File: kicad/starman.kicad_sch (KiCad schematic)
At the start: 244 parts, among them J1 M20-8771246, J10 PJ-063AH, J11 Conn_02x01, J2 M20-8771246, J3 M20-8771246, J4 ESW-106-44-T-S, J5 PH2-06-UA, J6 ESW-112-44-T-S, J7 Conn_01x10, J8 ESW-112-44-T-S, J9 Conn_01x10, SW1 PTS810 SJM 250 SMTR LFS, SW2 PTS810 SJM 250 SMTR LFS, SW3 SW_SPST, U1 ESP32-S2-MINI-1, U10 LED1642GWTTR, U11 AZ1084CS2-ADJ, U12 BA33BC0FP-E2, U13 PAM8302AAS, U2 LED1642GWTTR, U3 LED1642GWTTR, U4 LED1642GWTTR, U5 LED1642GWTTR, U6 LED1642GWTTR, U7 LED1642GWTTR, U8 LED1642GWTTR, U9 LED1642GWTTR, X1 ECS-2333-300, X2 ECS-2333-300, X3 ECS-2333-300

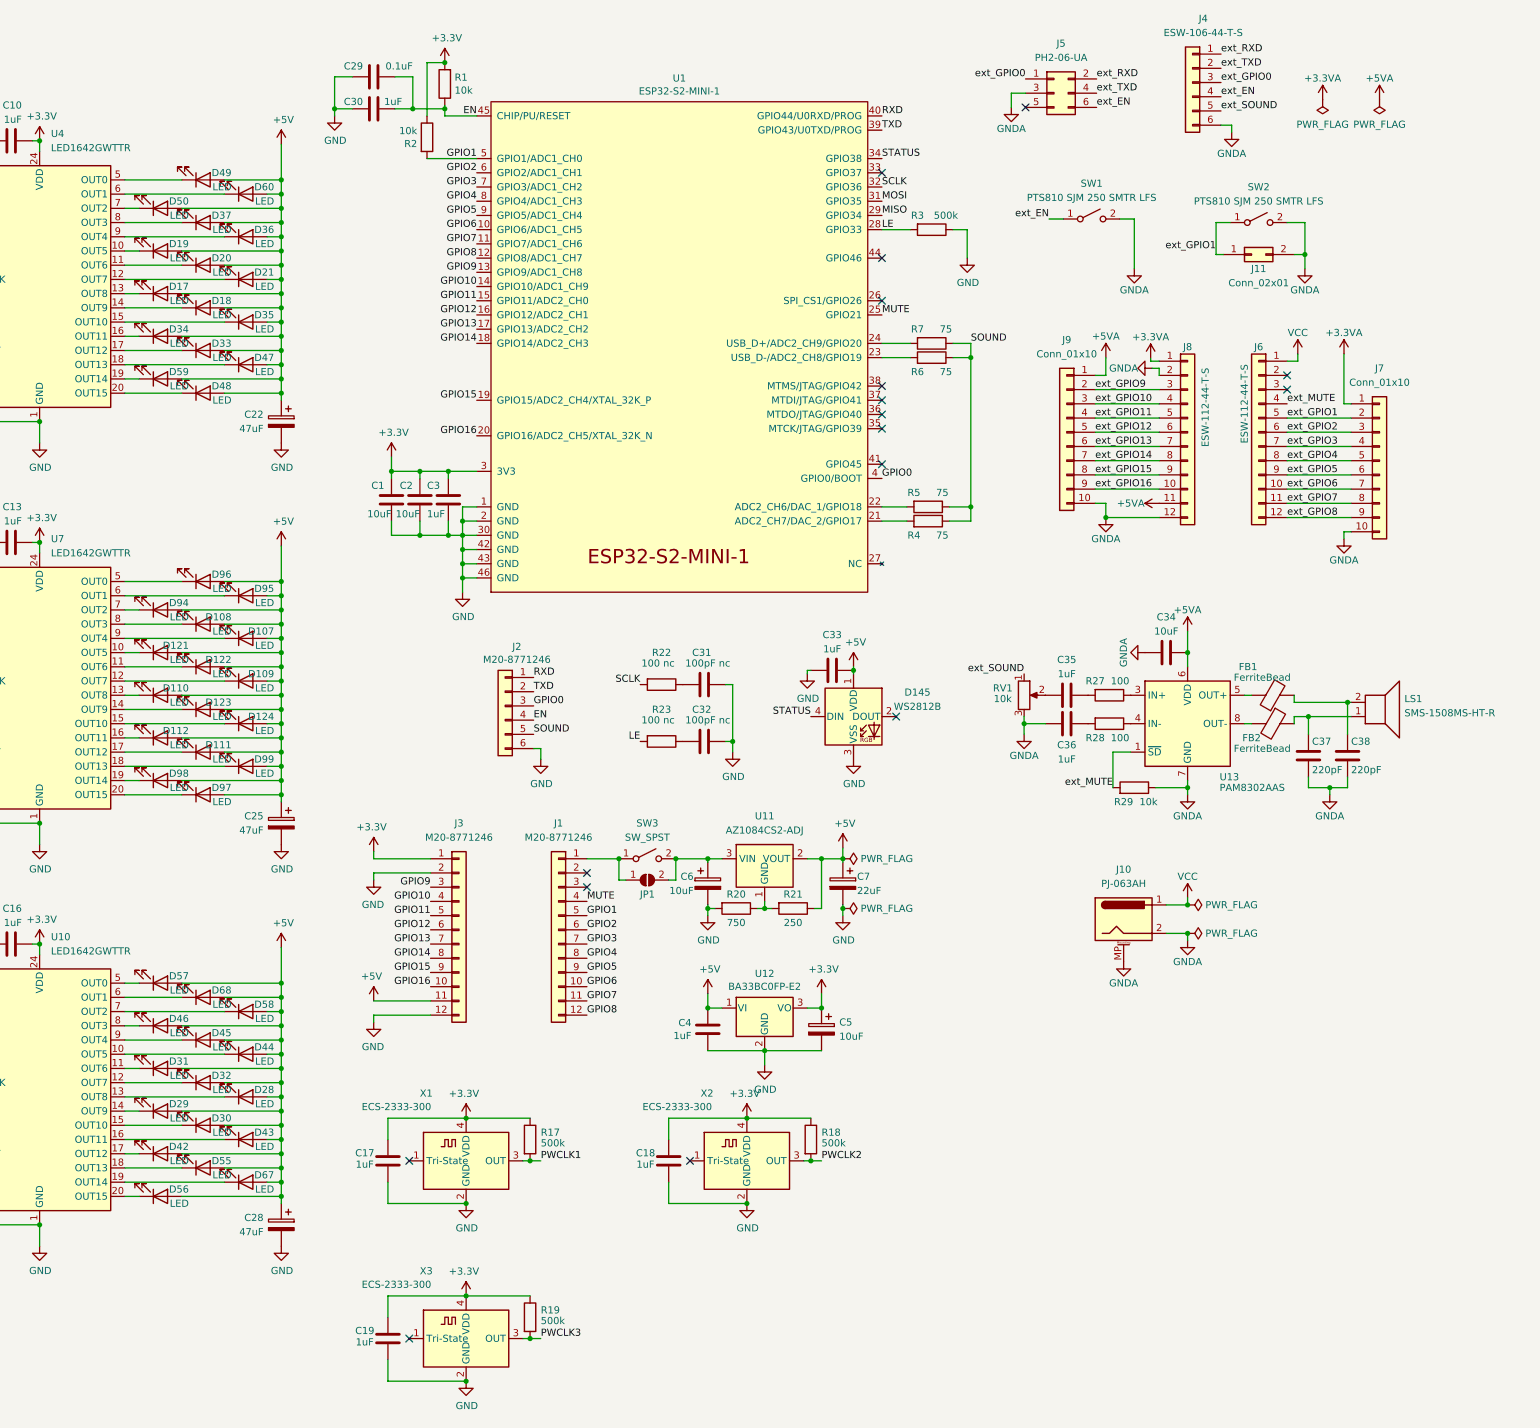
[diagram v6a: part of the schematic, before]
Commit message: Added on an optional mosfet and power switch
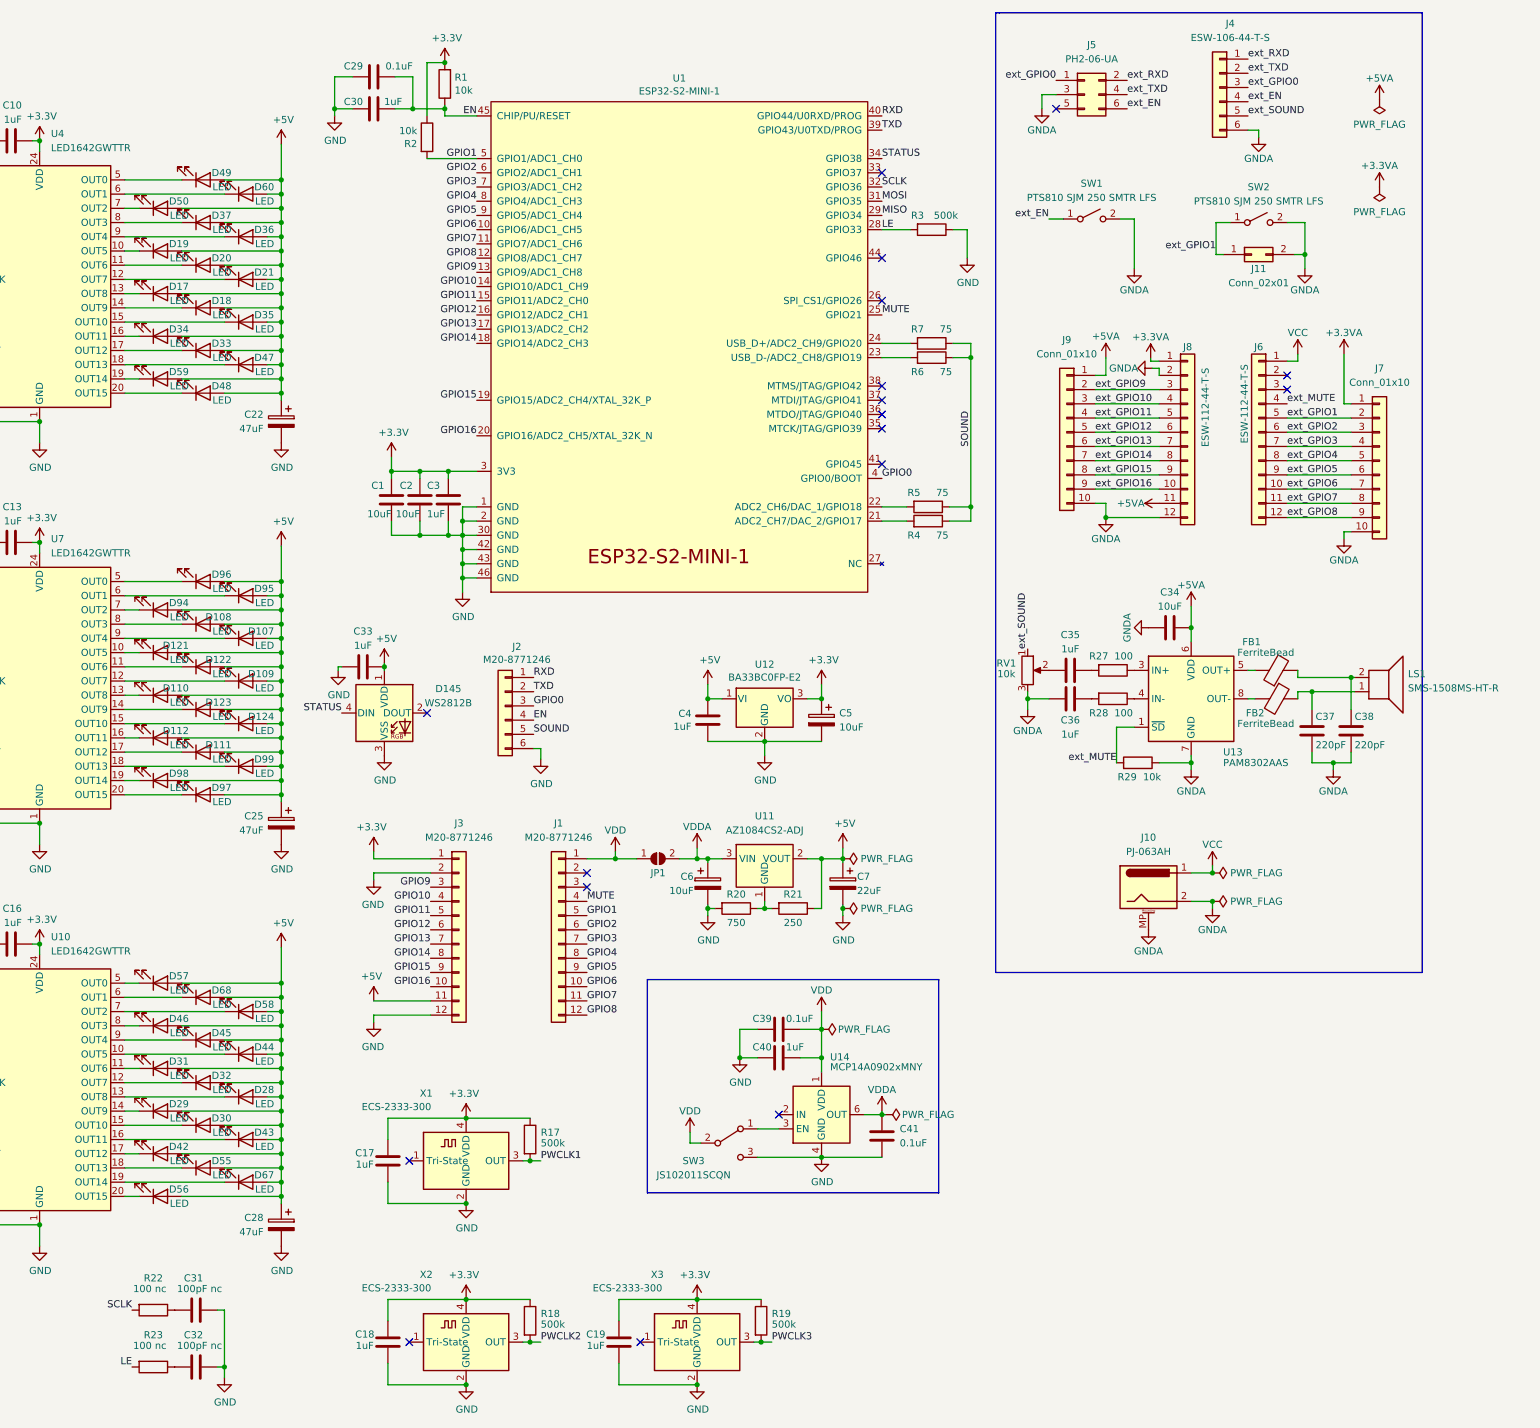
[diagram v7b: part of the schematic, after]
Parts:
- removed SW3: SW_SPST, Button_Switch_SMD:SW_DIP_SPSTx01_Slide_9.78x4.72mm_W8.61mm_P2.54mm, symbol Switch:SW_SPST
- added C39, C41: 0.1uF, Capacitor_SMD:C_0805_2012Metric, symbol Device:C
- added C40: 1uF, Capacitor_SMD:C_0805_2012Metric, symbol Device:C
- added SW3: JS102011SCQN, starman:SW_JS102011SCQN, symbol Switch:SW_SPDT
- added U14: MCP14A0902xMNY, Package_SO:SOIC-8_3.9x4.9mm_P1.27mm, symbol Driver_FET:MCP14A0902xMNY
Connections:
- net GND: now also C39.2, C40.2, C41.2, SW3.3 (C), U14.4 (GND), U14.5 (GND), U14.9 (GND)
- net VDD: now reaches J1.1 (Pin_1), JP1.1 (A)
- net VDD: now also C39.1, C40.1, SW3.2 (B), U14.1 (VDD), U14.8 (VDD)
- net VDDA: now reaches C6.1, JP1.2 (B), U11.3 (VIN)
- net VDDA: now also C41.1, U14.6 (OUT), U14.7 (OUT)
- new net: SW3.1 (A), U14.3 (EN)
- no-connect marks 17 -> 18
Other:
- moved on the sheet: C18, C19, C31, C32, C33, C34, C35, C36, C37, C38, C4, C5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

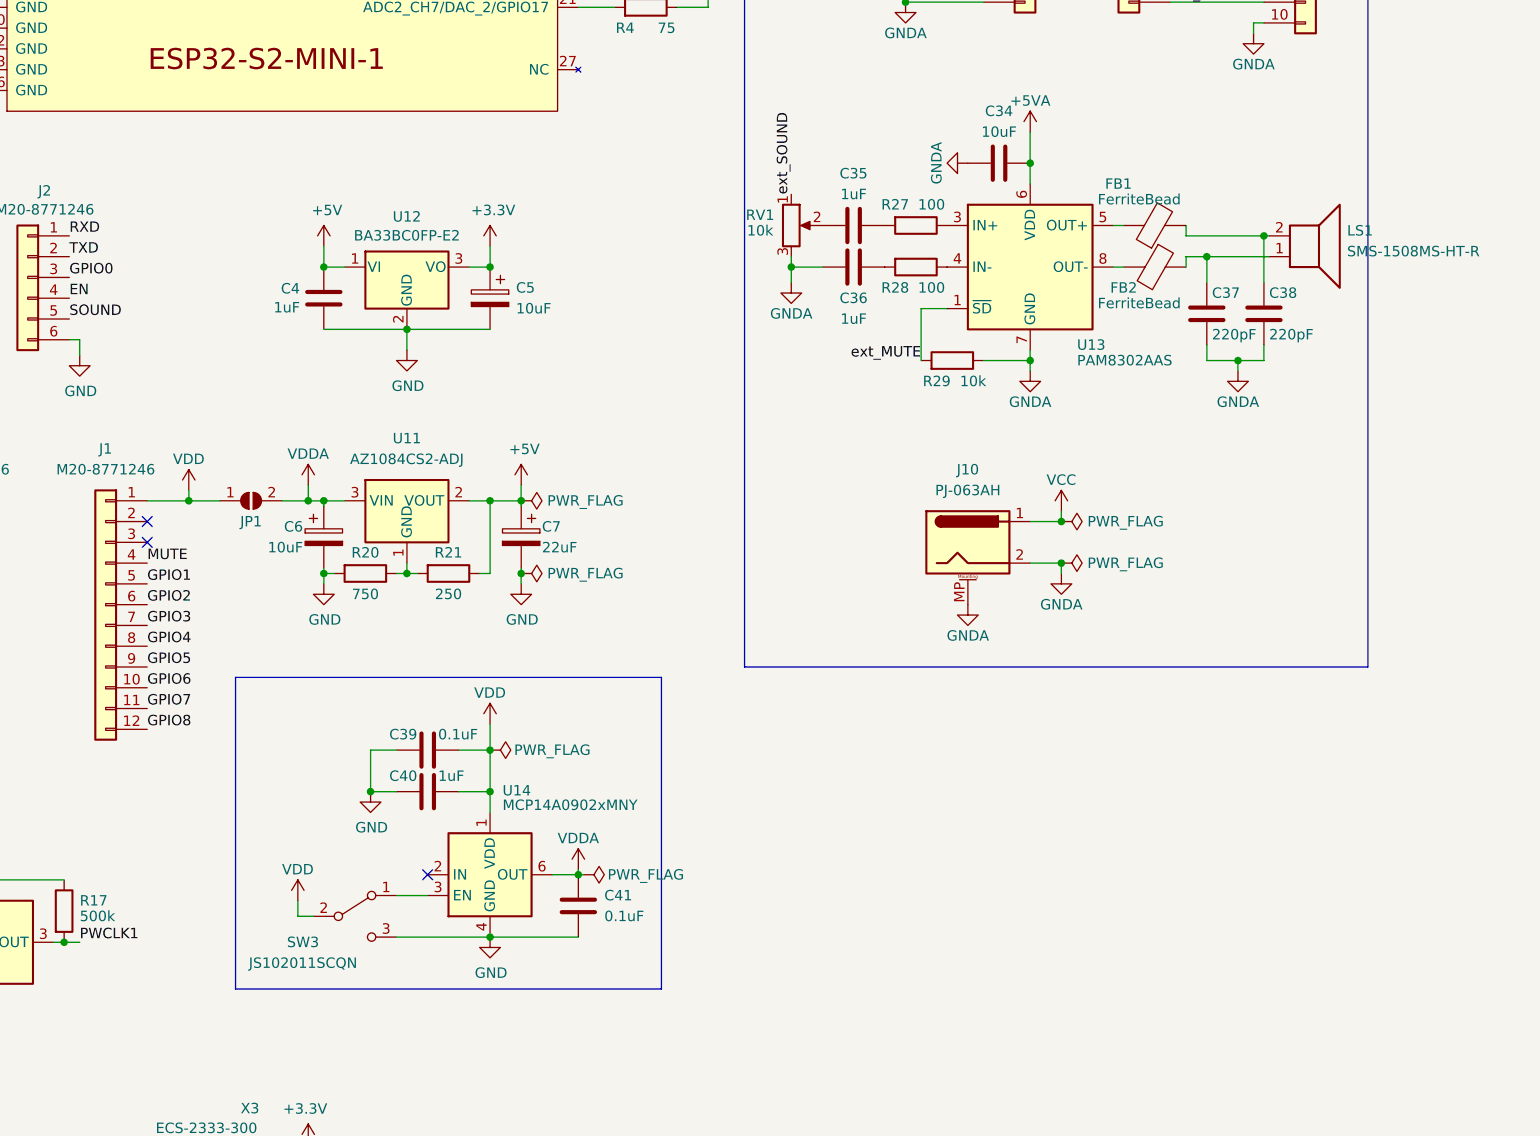
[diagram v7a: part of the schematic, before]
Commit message: Drop the mosfet/switch, run DRC
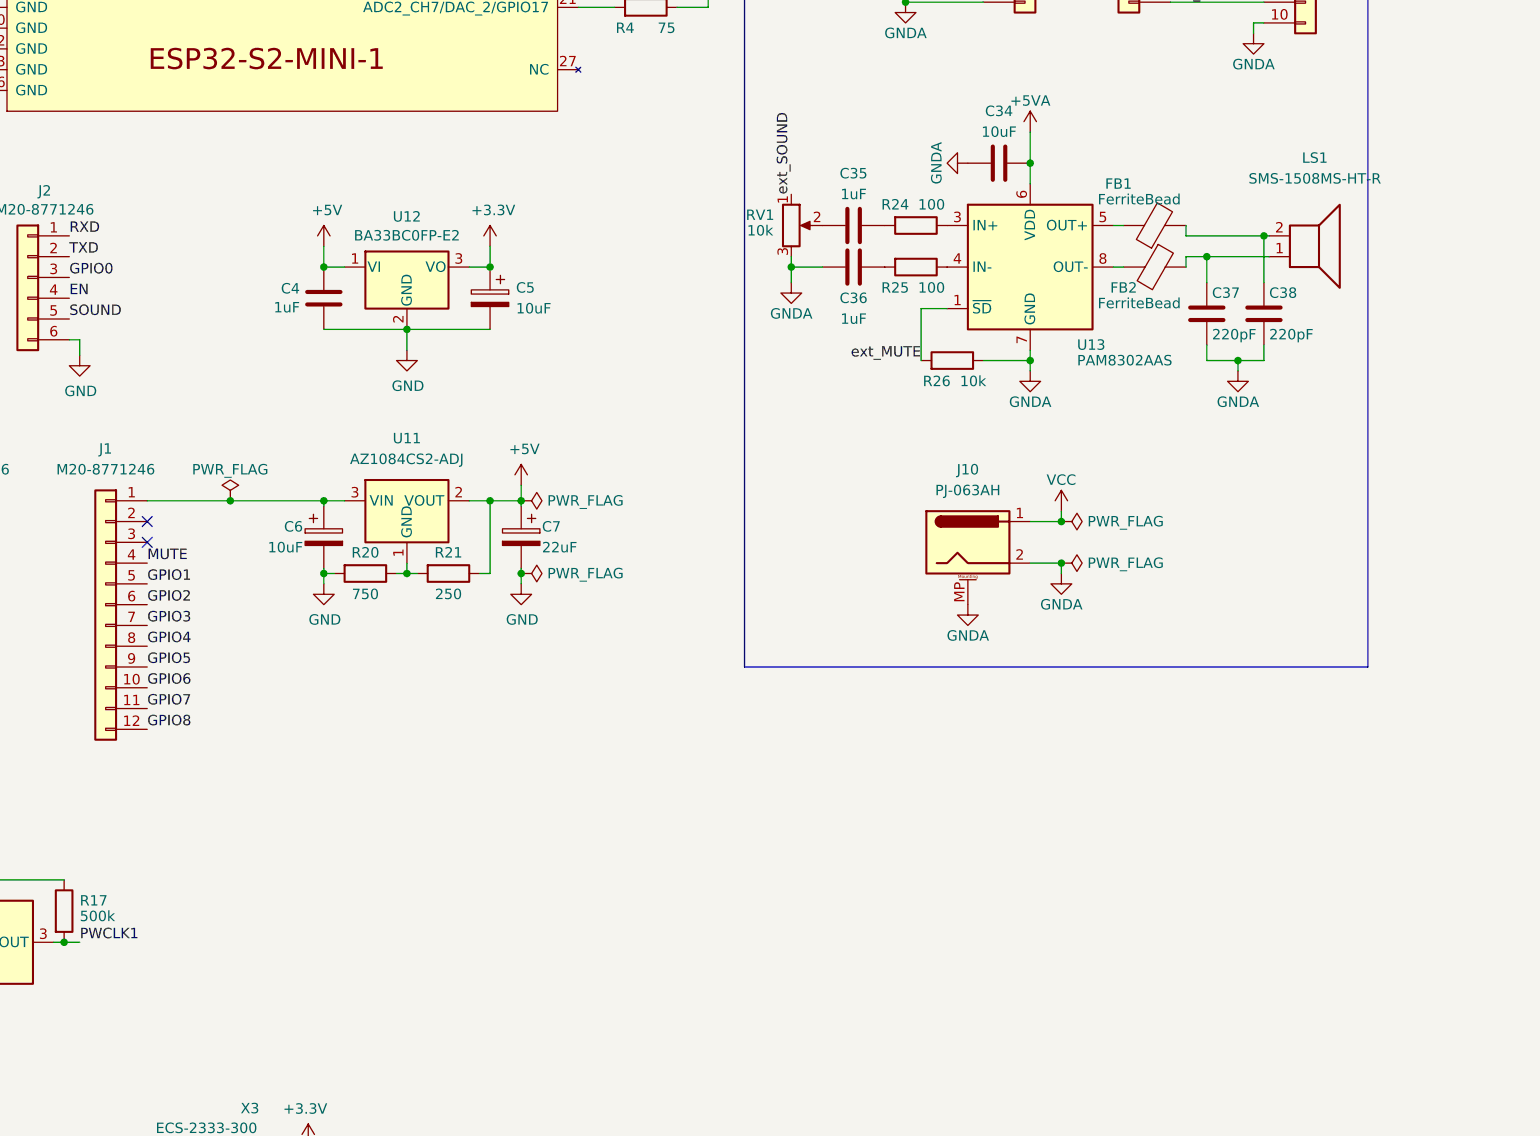
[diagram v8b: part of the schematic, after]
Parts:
- removed C39, C41: 0.1uF, Capacitor_SMD:C_0805_2012Metric, symbol Device:C
- removed C40: 1uF, Capacitor_SMD:C_0805_2012Metric, symbol Device:C
- removed JP1: SolderJumper_2_Open, Jumper:SolderJumper-2_P1.3mm_Open_RoundedPad1.0x1.5mm, symbol Jumper:SolderJumper_2_Open
- removed LS1: SMS-1508MS-HT-R, starman:SPKR_SMS-1508MS-HT-R, symbol Device:Speaker
- removed SW3: JS102011SCQN, starman:SW_JS102011SCQN, symbol Switch:SW_SPDT
- removed U14: MCP14A0902xMNY, Package_SO:SOIC-8_3.9x4.9mm_P1.27mm, symbol Driver_FET:MCP14A0902xMNY
- added LS1: SMS-1508MS-HT-R, starman:SPKR_SMS-1508MS-HT-R, symbol starman:SMS-1508MS-HT-R
- renumbered R27 to R24, R28 to R25, R29 to R26
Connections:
- net VDDA is gone; now on an unnamed net: C6.1, U11.3 (VIN)
- net at C38.1, FB1.2: now also LS1.2
- net at C37.1, FB2.1: now also LS1.1
- net VDD: no longer names the net of J1.1 (Pin_1)
- no-connect marks 18 -> 17
